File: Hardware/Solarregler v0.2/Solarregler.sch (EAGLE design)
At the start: 89 parts, among them IC1-1 STM32F105RBT6, IC2-1 MCP2551-E/SN or SN65HVD230D, IC2-2 J-LINK-10PIN-HOLES, IC2-3 PRTR5V0U4D, IC3-1 SIM1, IC3-2 MIC5209, IC5-1 MAX31865ATP+, IC5-2 MAX31865ATP+, IC6-1 MAX31865ATP+, Q1-1 8 MHz, Q1-2 32.768kHz, T3-1 PDTC124EU, U4 HUTSCHIENE_DEV

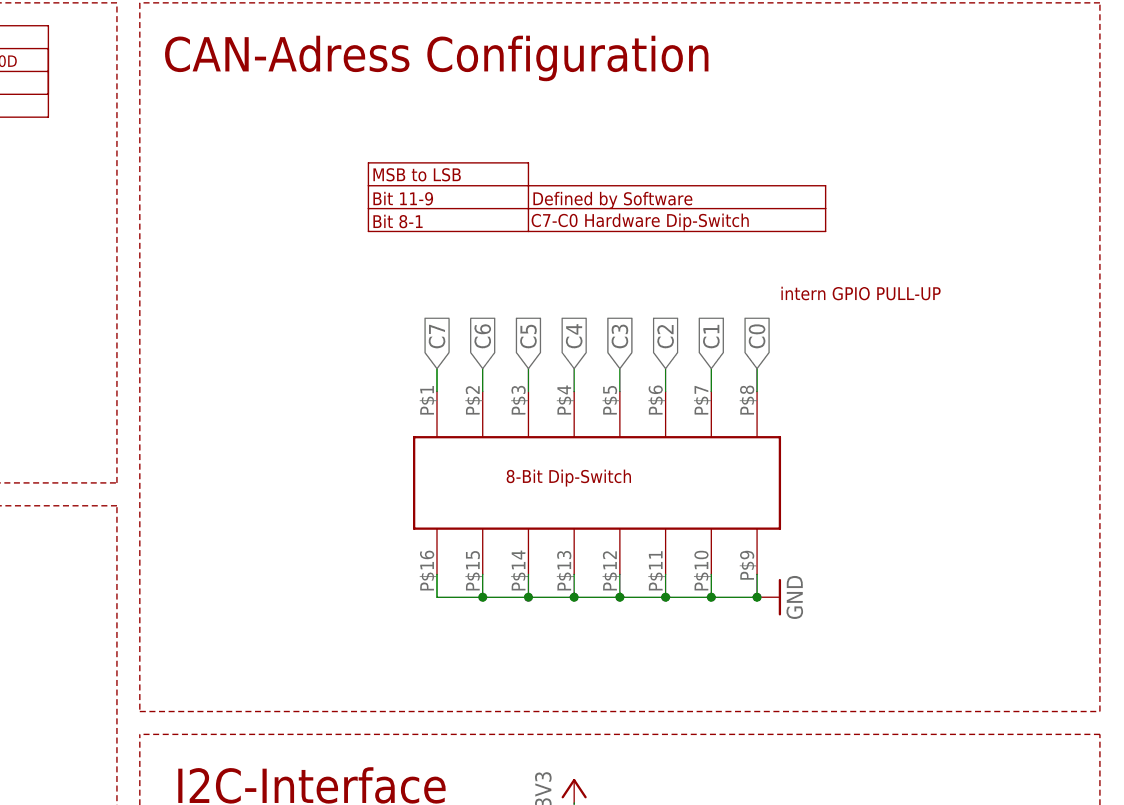
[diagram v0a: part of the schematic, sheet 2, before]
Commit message: Layout update nach Gespräch mit ME
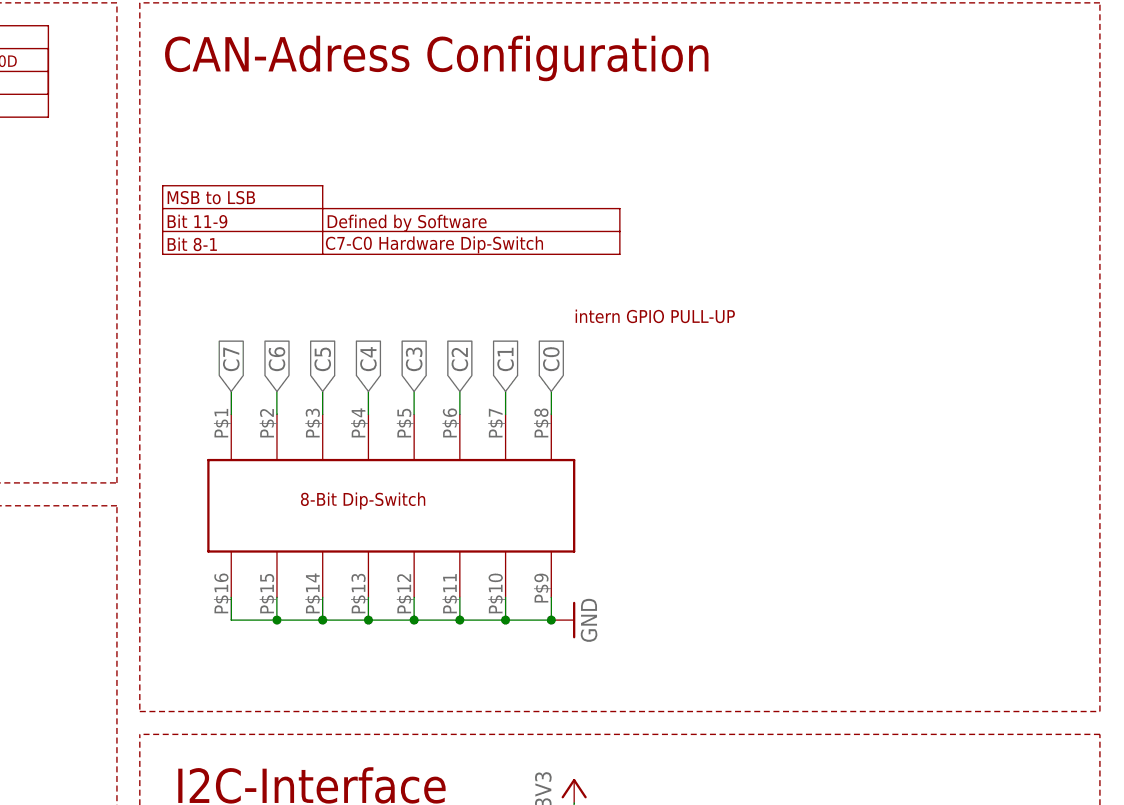
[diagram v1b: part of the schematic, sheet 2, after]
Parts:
- removed U$3: FINDER_36.11, 000_eigene_Bauteile:FINDER_36.11
- added U$2: FINDER_34.51, 000_eigene_Bauteile:FINDER_34.51
- D3-3: device diode:DIODE-MELF-MLL41 -> diode:DIODE-SMB
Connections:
- net +5V: now also U$2.A1; no longer U$3.A1
- net N$10: now also U$2.A2; no longer U$3.A2
- net RELAIS_COM: now also U$2.11; no longer U$3.11
- net RELAIS_NC: now also U$2.12; no longer U$3.12
- net RELAIS_NO: now also U$2.13; no longer U$3.14
